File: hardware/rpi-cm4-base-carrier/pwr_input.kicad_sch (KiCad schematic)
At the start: 17 parts, among them IC2 LM74610QDGKRQ1, IC3 LM74610QDGKRQ1

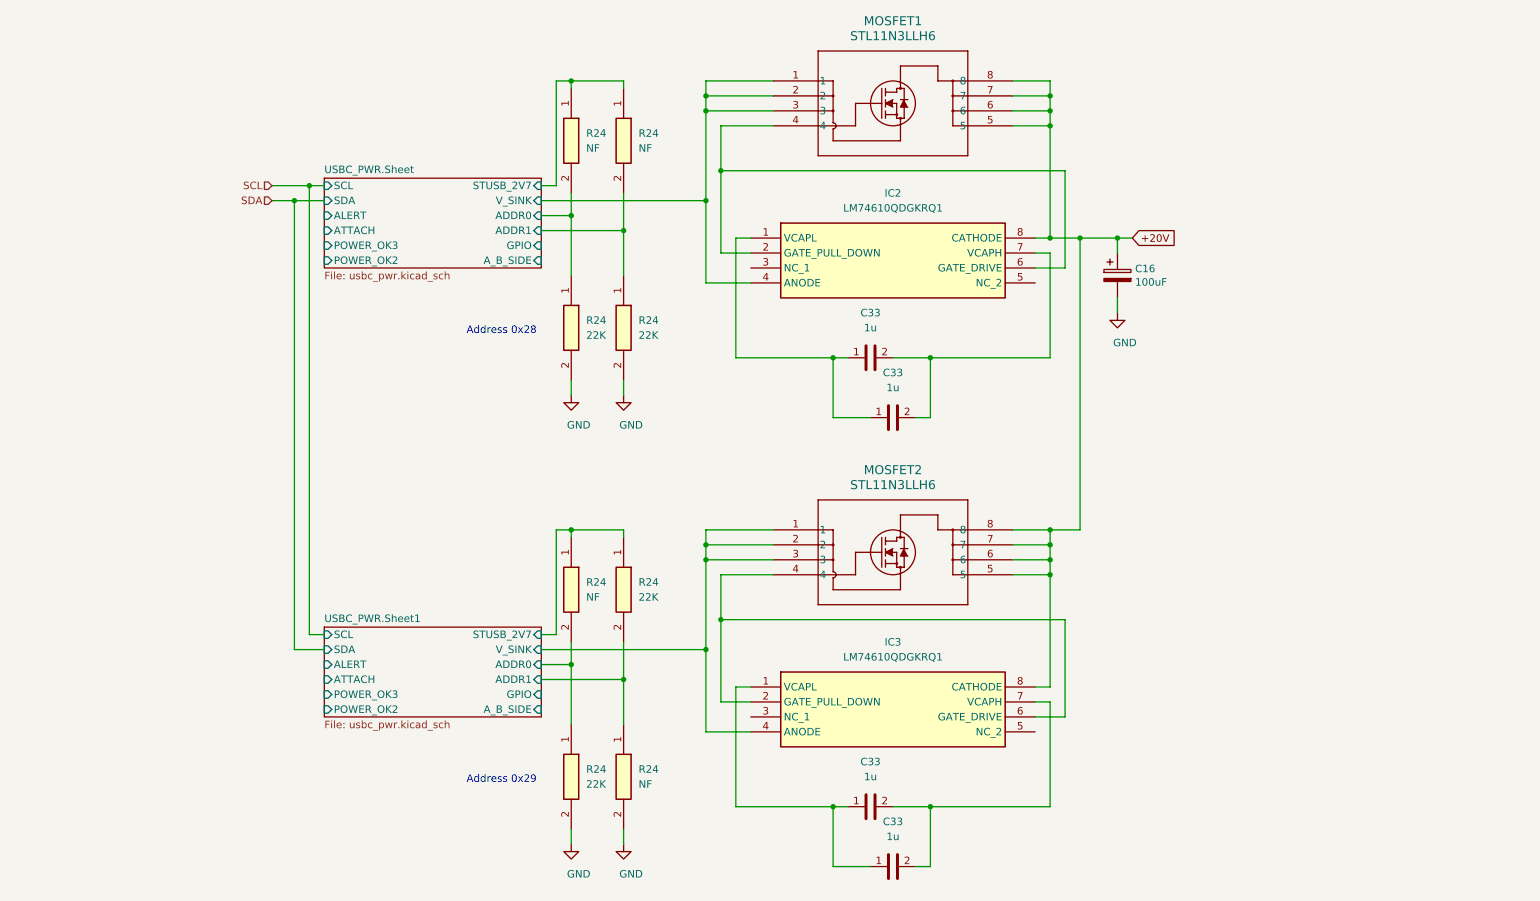
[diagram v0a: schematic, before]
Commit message: PWR regs complete, EMI protection? LDO low noise passthrough??
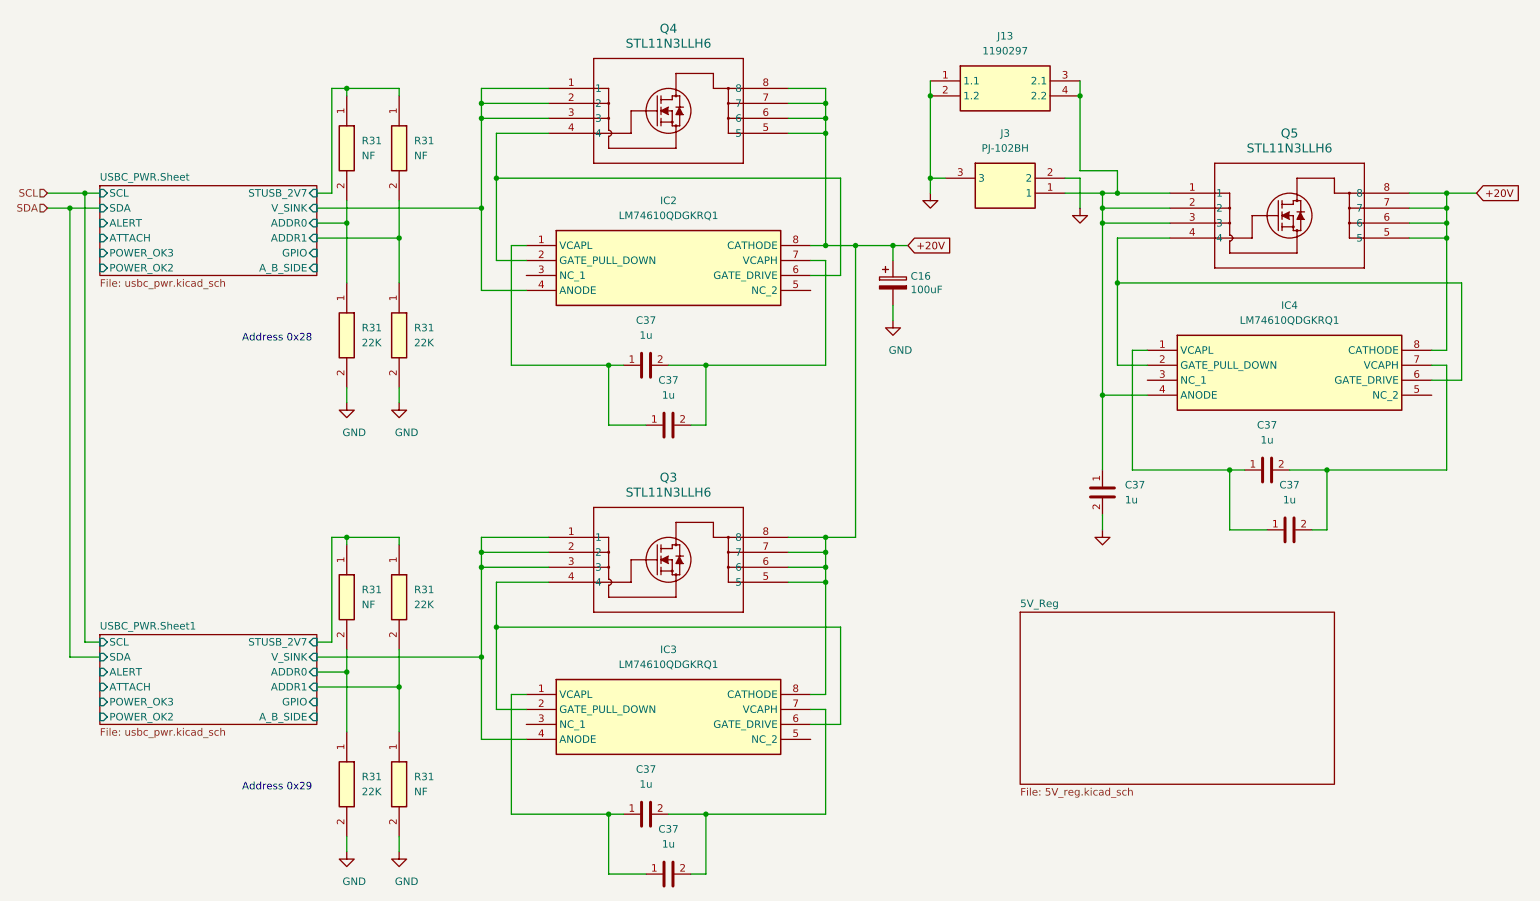
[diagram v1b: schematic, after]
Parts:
- removed MOSFET1, MOSFET2: STL11N3LLH6, STL11N3LLH6:POWERFLAT_3P3X3P3_STM, symbol STL11N3LLH6:STL11N3LLH6
- added C37 (x3): 1u, RESC2012X140N:RESC2012X140N, symbol 08055C105JAT2A:08055C105JAT2A
- added IC4: LM74610QDGKRQ1, SamacSys_Parts:SOP65P490X110-8N, symbol SamacSys_Parts:LM74610QDGKRQ1
- added J13: 1190297, 1190297, symbol SamacSys_Parts:1190297
- added J3: PJ-102BH, PJ-102AH, symbol SamacSys_Parts:PJ-102BH
- added Q3, Q4, Q5: STL11N3LLH6, POWERFLAT_3P3X3P3_STM, symbol STL11N3LLH6:STL11N3LLH6
- renumbered C33 to C37, R24 to R31
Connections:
- net +20V: now also IC4.8 (CATHODE), Q3.5, Q3.6, Q3.7, Q3.8, Q4.5, Q4.6, Q4.7, Q4.8, Q5.5, Q5.6, Q5.7, Q5.8
- net GND: now also C37.2, J13.1 (1.1), J13.2 (1.2), J3.2, J3.3
- net USBC_PWR.Sheet/V_SINK: now also Q4.1, Q4.2, Q4.3
- net USBC_PWR.Sheet1/V_SINK: now also Q3.1, Q3.2, Q3.3
- net at IC2.2 (GATE_PULL_DOWN), IC2.6 (GATE_DRIVE): now also Q4.4
- net at IC3.2 (GATE_PULL_DOWN), IC3.6 (GATE_DRIVE): now also Q3.4
- new net: C37.1, IC4.4 (ANODE), J13.3 (2.1), J13.4 (2.2), J3.1, Q5.1, Q5.2, Q5.3
- new net: C37.1, C37.1, IC4.1 (VCAPL)
- new net: C37.2, C37.2, IC4.7 (VCAPH)
- new net: IC4.2 (GATE_PULL_DOWN), IC4.6 (GATE_DRIVE), Q5.4
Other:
- added sheet 5V_Reg (5V_reg.kicad_sch)
- moved on the sheet: C16, C37, IC2, IC3, R31

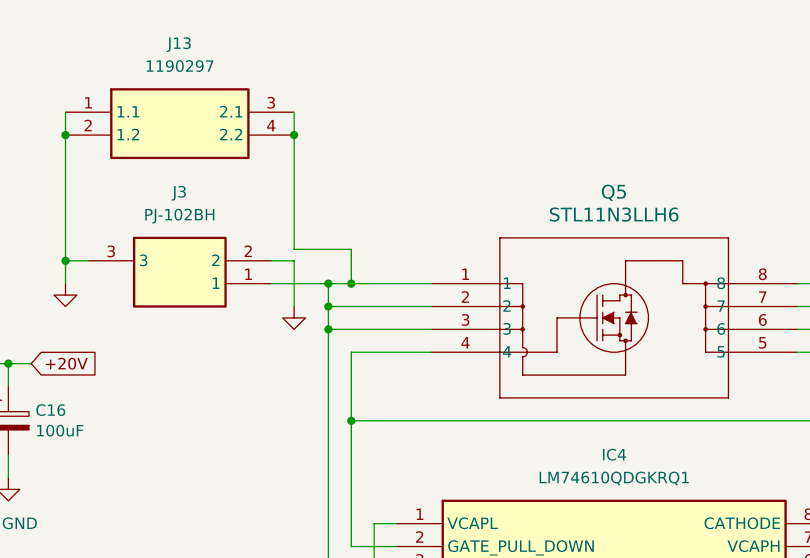
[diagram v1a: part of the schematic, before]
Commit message: layout ready for review as major components now complete
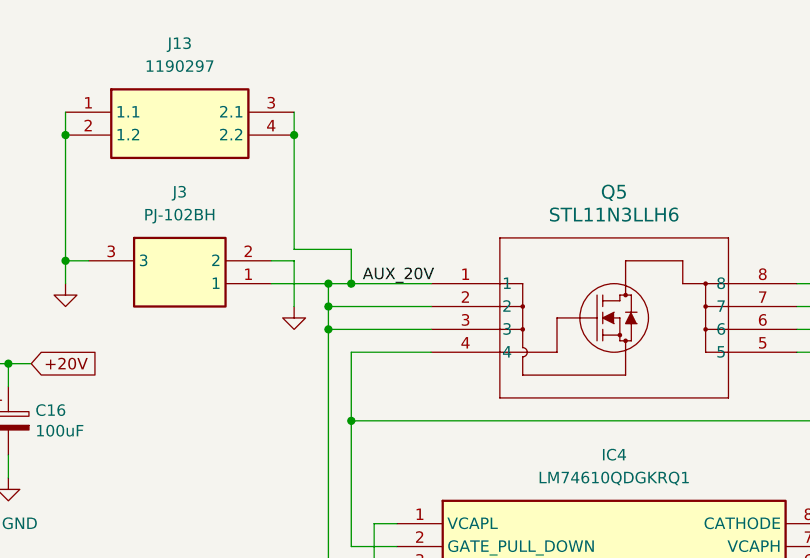
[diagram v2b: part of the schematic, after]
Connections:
- net AUX_20V: now reaches C37.1, IC4.4 (ANODE), J13.3 (2.1), J13.4 (2.2), J3.1, Q5.1, Q5.2, Q5.3
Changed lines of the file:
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@@
+    (effects (font (size 1.27 1.27)) (justify left bottom))
+  )
+  (label "AUX_20V" (at 201.93 41.91 0) (fields_autoplaced)
     (effects (font (size 1.27 1.27)) (justify left bottom))
   )

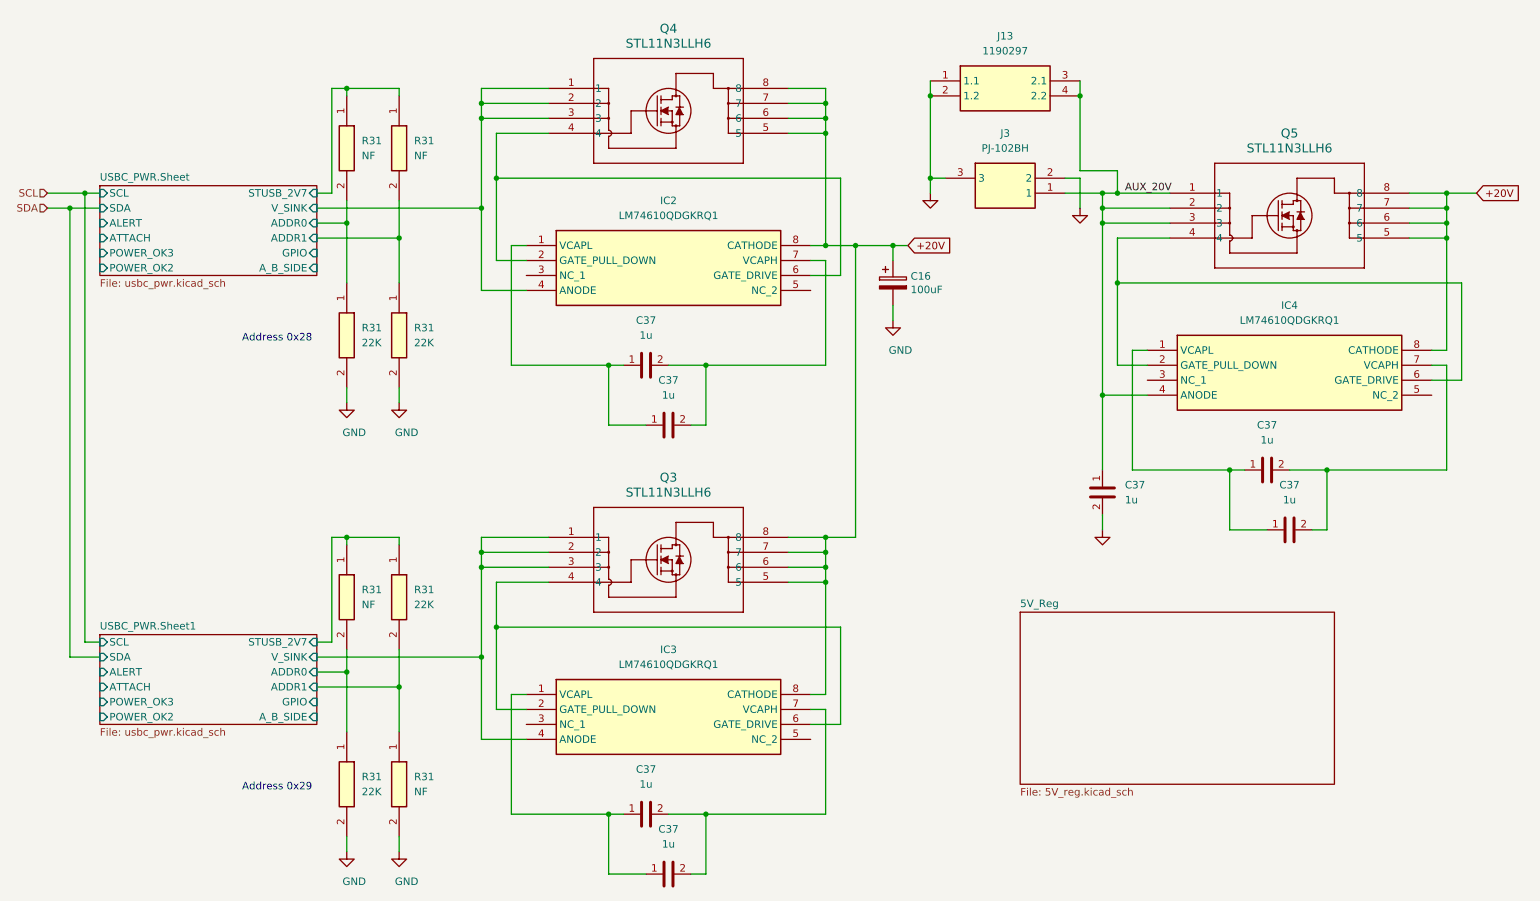
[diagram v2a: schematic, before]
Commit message: convert IC refs to U refs and re-annotate, add fiducials and extra via stitching to layout
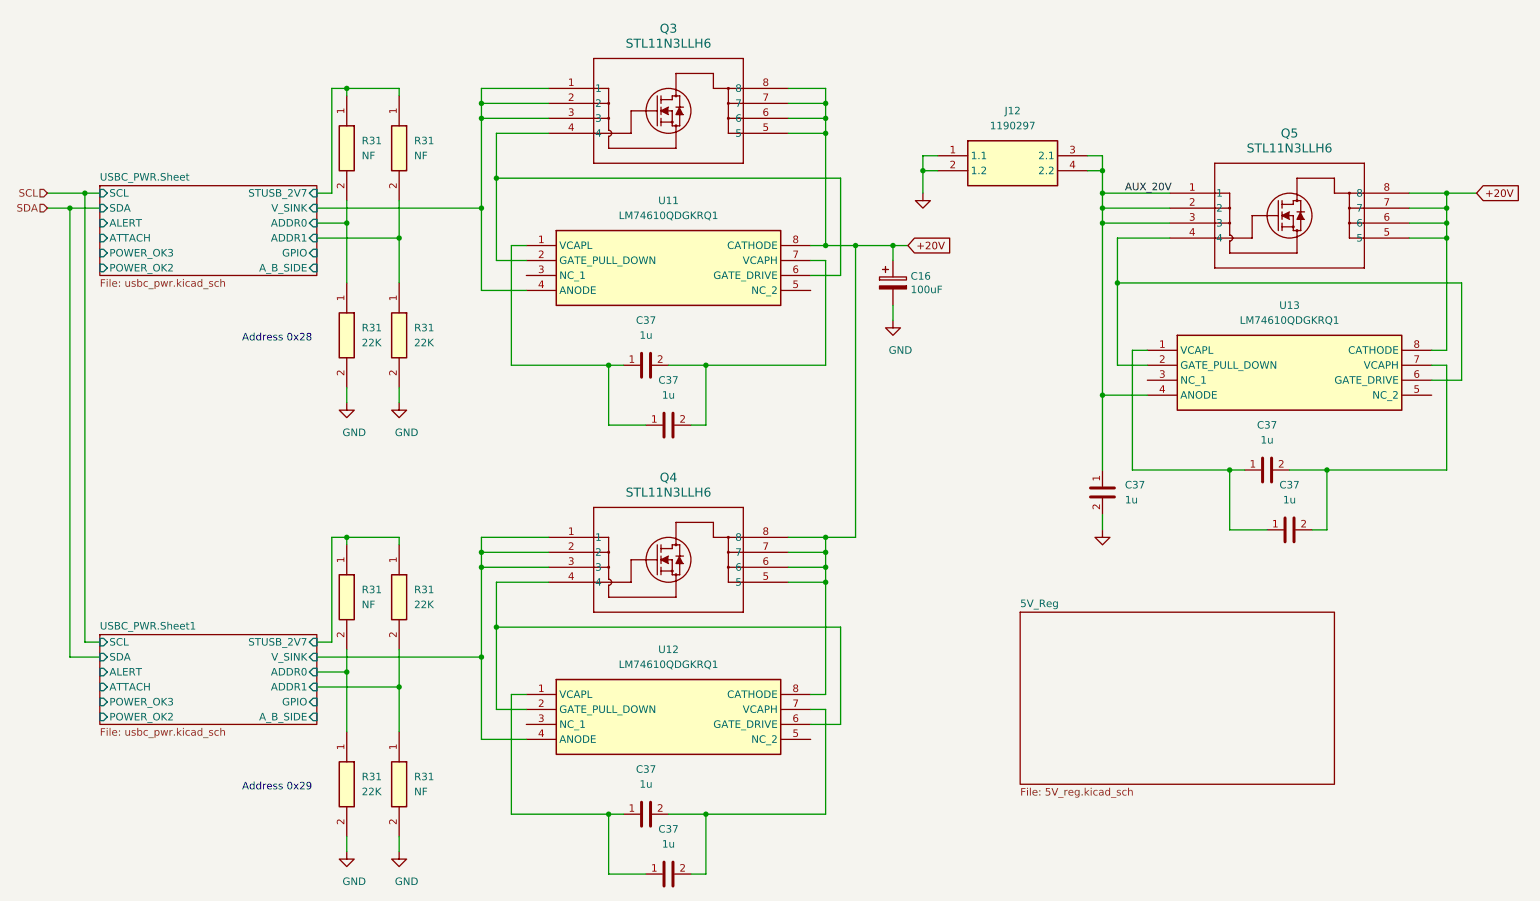
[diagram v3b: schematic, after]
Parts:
- removed J3: PJ-102BH, PJ-102AH, symbol SamacSys_Parts:PJ-102BH
- U11: renamed from IC2; footprint SamacSys_Parts:SOP65P490X110-8N -> SOP65P490X110-8N
- U12: renamed from IC3; footprint SamacSys_Parts:SOP65P490X110-8N -> SOP65P490X110-8N
- U13: renamed from IC4; footprint SamacSys_Parts:SOP65P490X110-8N -> SOP65P490X110-8N
- renumbered J13 to J12, Q4 to Q3, Q3 to Q4
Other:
- moved on the sheet: J12

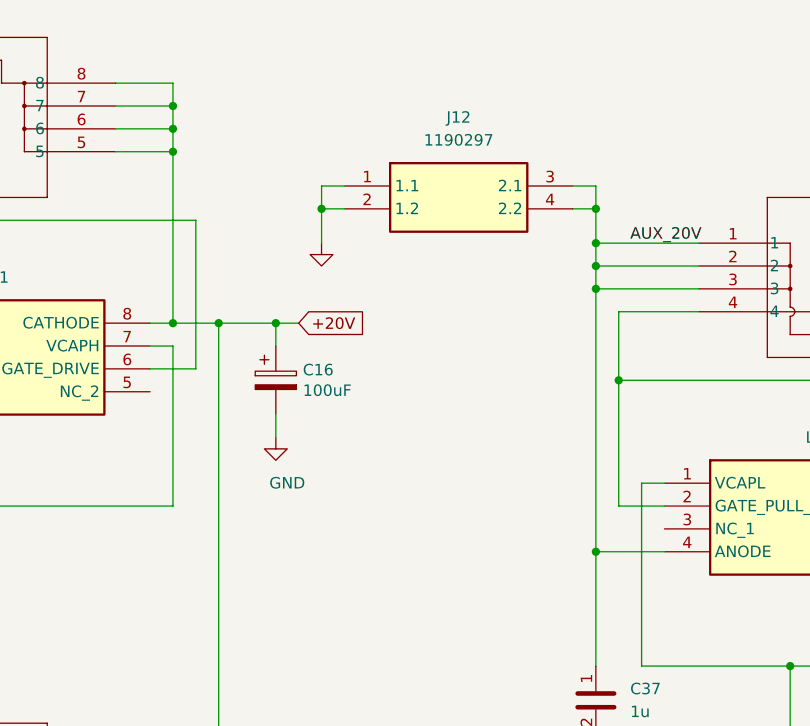
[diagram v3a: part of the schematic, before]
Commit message: design files exported ready for manufacture, LCSC part numbers added throughout the library
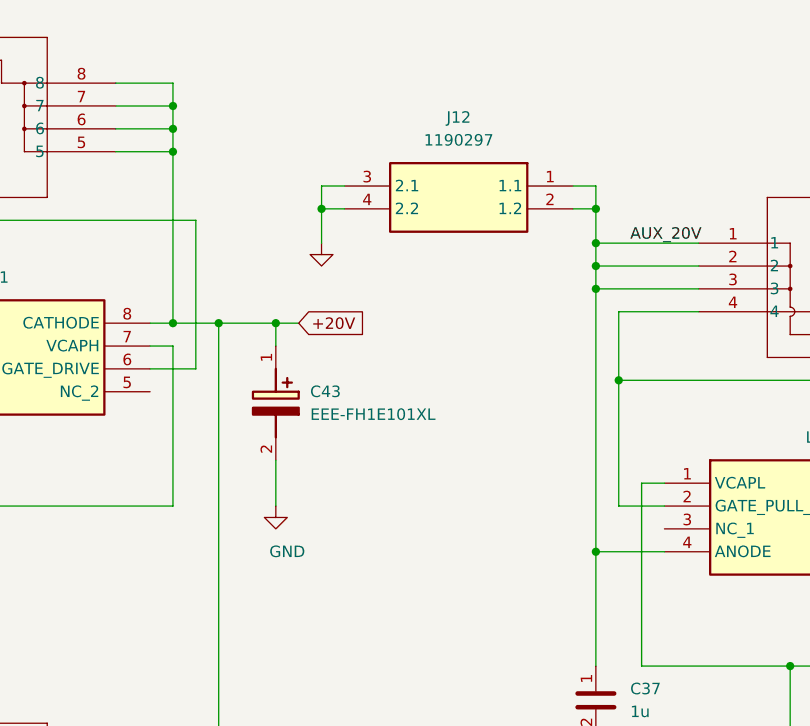
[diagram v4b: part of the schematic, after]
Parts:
- removed C16: 100uF, Capacitor_Tantalum_SMD:CP_EIA-7343-31_Kemet-D, symbol Device:CP
- added C43: EEE-FH1E101XL, EEEHP1H4R7P, symbol SamacSys_Parts:EEE-FH1E101XL
- C37: LCSC Part # (none) -> C1849853; LCSC Part Number (none) -> C1849853
- J12: LCSC Part # (none) -> C3308983; LCSC Part Number (none) -> C3308983
- Q3, Q4, Q5: LCSC Part # (none) -> C2965326; LCSC Part Number (none) -> C2965326
- R31: LCSC Part # (none) -> NF; LCSC Part Number (none) -> NF
- R31: LCSC Part # (none) -> C2576480; LCSC Part Number (none) -> C2576480
- U11, U12, U13: LCSC Part # (none) -> C2649431; LCSC Part Number (none) -> C2649431
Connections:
- net +20V: now also C43.1 (+)
- net AUX_20V: now also J12.1 (1.1), J12.2 (1.2); no longer J12.3 (2.1), J12.4 (2.2)
- net GND: now also J12.3 (2.1), J12.4 (2.2), C43.2 (-); no longer J12.1 (1.1), J12.2 (1.2)
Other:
- title: (none) -> Raspberry Pi Compute Module 4 Control Node
